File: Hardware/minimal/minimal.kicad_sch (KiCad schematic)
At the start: 26 parts, among them J101 USB_C_Receptacle_USB2.0_16P, SW101 SW_SPST, U101 KTM1331TD-ST3, U102 USBLC6-2P6, U103 TLV76733DRVx, U104 TLV76733DRVx

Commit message: Commit DC-coupled TAC5112 design
This is a slightly modified 'minimal' board with the same board outline
but an added 3.5mm DC jack.

The upside: no coupling capacitors into the codec that have distortion
at low-end frequencies due to the capacitors' voltage coefficients.  The
existing 0805 4.7uF caps were large for this minimal board, and caused
the THD+N to go to roughly -65dB for a low-B bass signal at a reasonable
signal level of 0.1Vrms.  That's not horrible, but it's not optimal.

The 10Hz corner also caused issues for using the pedal as a measurement
instrument, since it introduced a consistent measurement error that was
initially incorrectly attributed to the pedal under test.

The other upside is simply the existence of the headphone jack.  That
user-visible addition is likely a lot more noticeable than the
low-frequency THD+N improvement this should bring or the improvement in
low-end frequency response.

Downside: the TAC212 with a better noise floor is out of stock, and so I
am back to the slightly lower dynamic range of the TAC5112 - but with
the new fixed footprint with proper paste and thermal vias.  The thermal
pad is likely to actually come into play now that the codec is used as a
headphone amplifier too.

The lower dynamic range is unlikely to be noticeable - it wasn't on the
original mono boards (the added noise was probably entirely due to the
negative inputs having been left floating on that board).

And I'll need to route i2c again, and it's an entirely new untested
configuration.  I've added a trace to route one of the TAC5112 GPIOs
just in case it comes in useful - possibly as an ASI error reporting
interrupt line.

The default codec routing for that new pin being routed is as an
interrupt output: driven low with a weak pull-up.  It's routed to GPIO15
on the rp2354, which hardware in turn defaults to a weak pull-down,
disconnected from any logic.

So without any firmware, this ends up being a few microamps of current
on that trace due to the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
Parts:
- added R105, R106: 5k1, Resistor_SMD:R_0402_1005Metric, symbol Device:R
- D102, D103: value WS2812B-4020 -> WS2812B-4020-V6; footprint Mylib:WS2812B-4020 -> Mylib:WS2812B-4020-V6; symbol Mylib:WS2812B-4020 -> Mylib:WS2812B-4020-V6; LCSC PN C965557 -> C52941387; MANUFACTURER_PART_NUMBER WS2812B-4020 -> WS2812B-4020-V6
- R104: value 10R -> 1R; footprint Resistor_SMD:R_0402_1005Metric -> Resistor_SMD:R_0603_1608Metric; LCSC PN C25077 -> C22936; MANUFACTURER_PART_NUMBER 0402WGF100JTCE -> 0603WAF100KT5E
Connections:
- net +3.3VA: now also C105.1
- net +3V3: now also R105.1, R106.1
- net GPIO16: now also R106.2
- net GPIO17: now also R105.2
- net +5VA: no longer names the net of C106.1, L101.2, U103.6 (IN)
- net +5VA: no longer C105.1
- no-connect marks 28 -> 23
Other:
- sheet TAC5242 renamed TAC5212
- sheet TAC5212 ports: added OUT1M, OUT2M, TAC_GPIO1, TAC_SCL, TAC_SDA; removed none
- note added: "Stereo guitar pedal with RP2354A MCU and a TAC5212 codec Controlled over MIDI over USB. Two smart LEDs for status, and 8MB of QSPI PSRAM."
- note removed: "Stereo guitar pedal with RP2354A MCU and a TAC5242 codec Controlled over MIDI over USB. Two smart LEDs for status, and 8MB of QSPI PSRAM."
- moved on the sheet: C105, C106, C109, U103

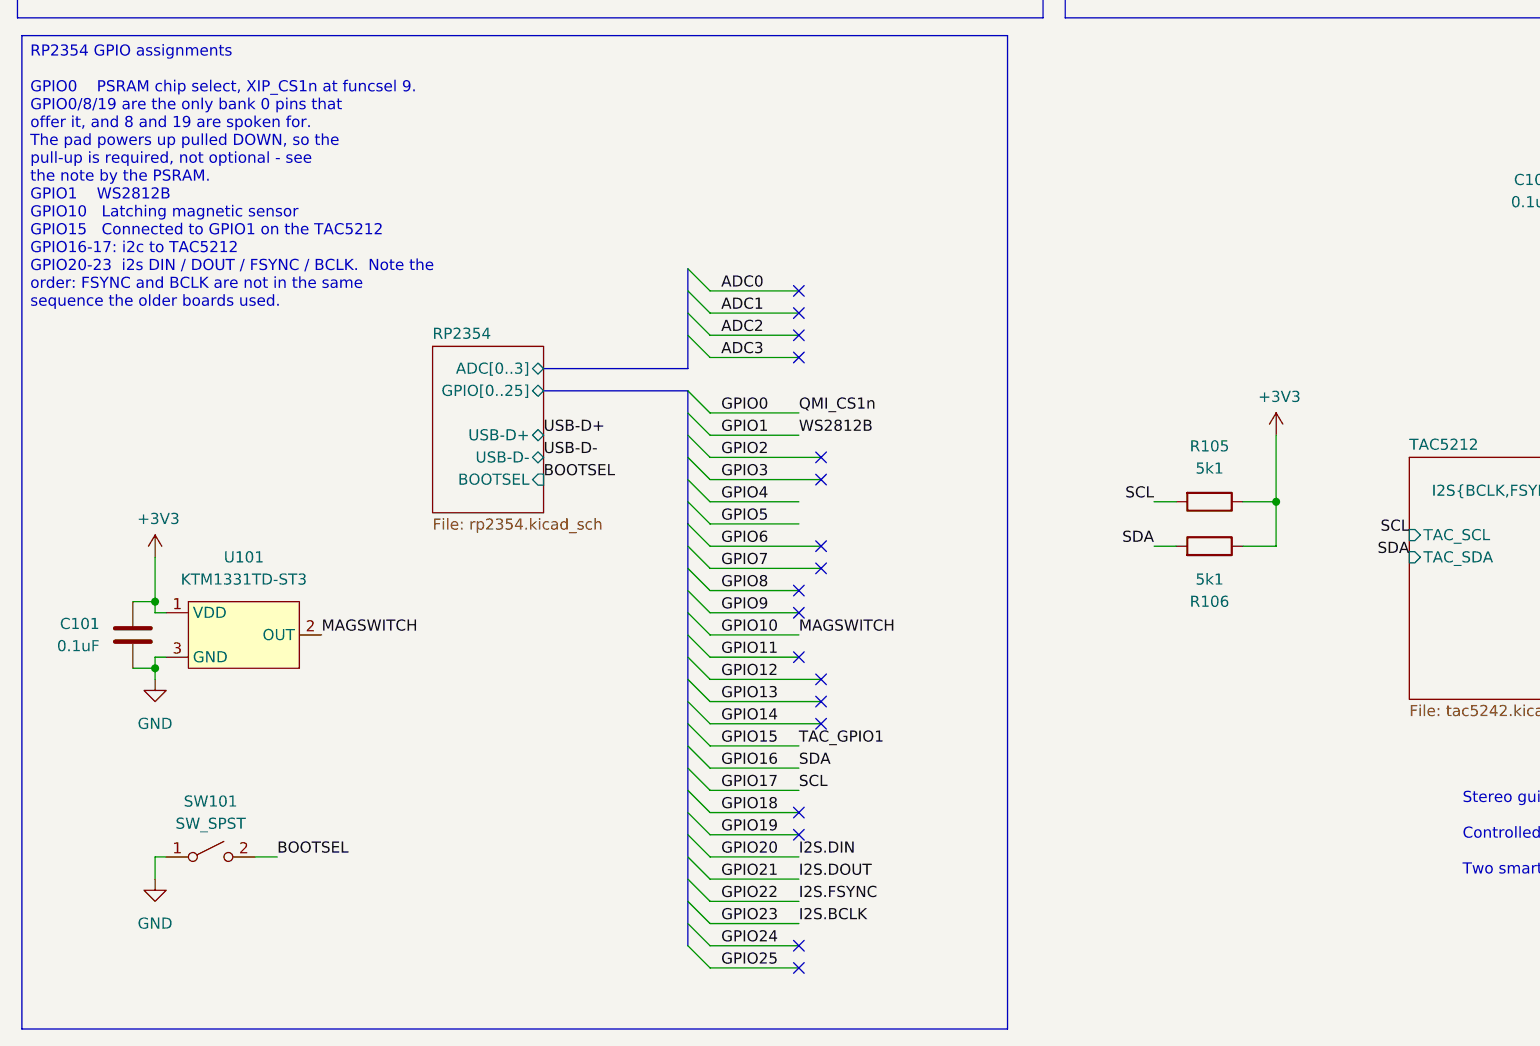
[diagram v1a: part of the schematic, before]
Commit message: Update the minimal board with a nRF54L10 BLE chip
Let's see how this works.  It needs more sanity checking, but looks like
it might be workable, and it fits under the output jack which was mostly
empty space before.

The rp2354 still acts as the i2s master - now for both the TAC5112 and
the nRF54.  It also will act as the SWD programmer for the new Nordic
Semi chip.  So all programming still happens over the USB-C port, it's
just that you first need to teach the rp2354 how to program the nRF54.

That's probably a whole separate firmware part where the rp2354
temporarily just acts as a SWD programmer before it goes back to being a
guitar pedal.

The firmware side will be "interesting".  I've done a nRF52840 chip
before, and didn't exactly enjoy the strange Nordic SDK.  And the nRF54
SDK is very different with either a Zephyr model or a bare metal option
that looks more like the traditional one.  But it looks like if I want
to do BLE audio, I will need to use that Zephyr one.

That's a problem for another day.  But I have SWD, an UART, and a
separate set of i2s pins wired up to talk to the nRF54, so it should all
be just a small matter of programming.  If the hardware works.

Signed-off-by: Linus Torvalds <torvalds@linux-foundation.org>
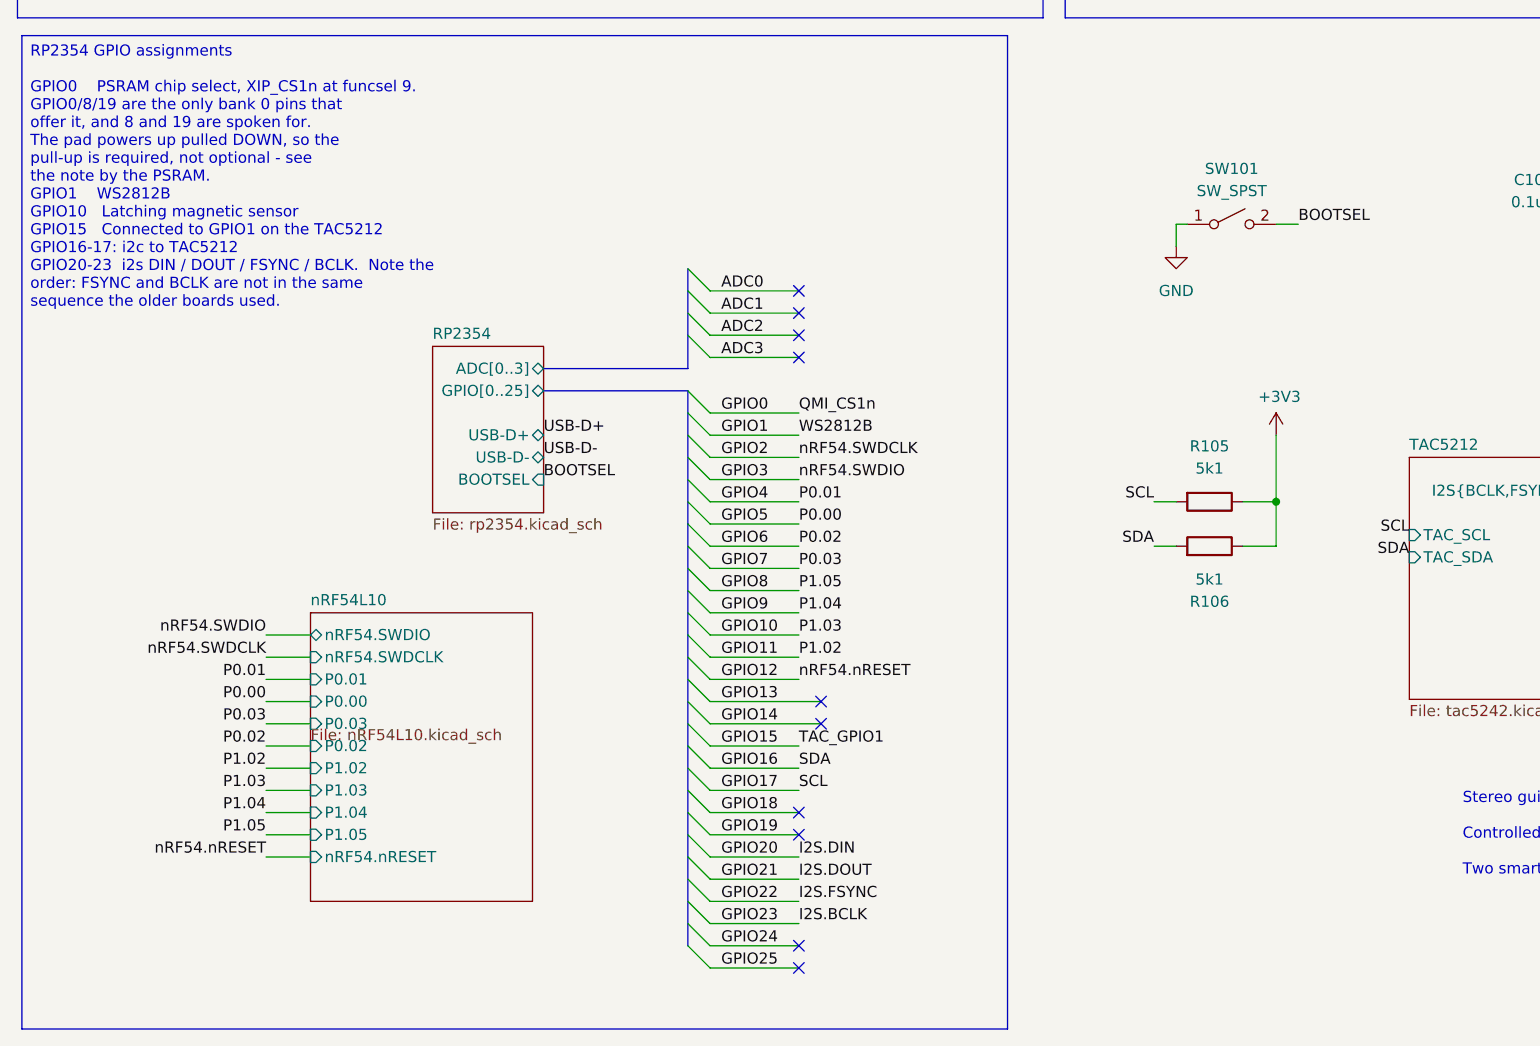
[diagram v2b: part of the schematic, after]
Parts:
- removed C101: 0.1uF, Capacitor_SMD:C_0402_1005Metric, symbol Device:C
- removed U101: KTM1331TD-ST3, Package_TO_SOT_SMD:SOT-23, symbol Mylib:KTM1331TD-ST3
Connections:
- no-connect marks 23 -> 15
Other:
- added sheet nRF54L10 (nRF54L10.kicad_sch)
- moved on the sheet: SW101
